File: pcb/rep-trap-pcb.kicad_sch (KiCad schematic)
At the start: 0 parts

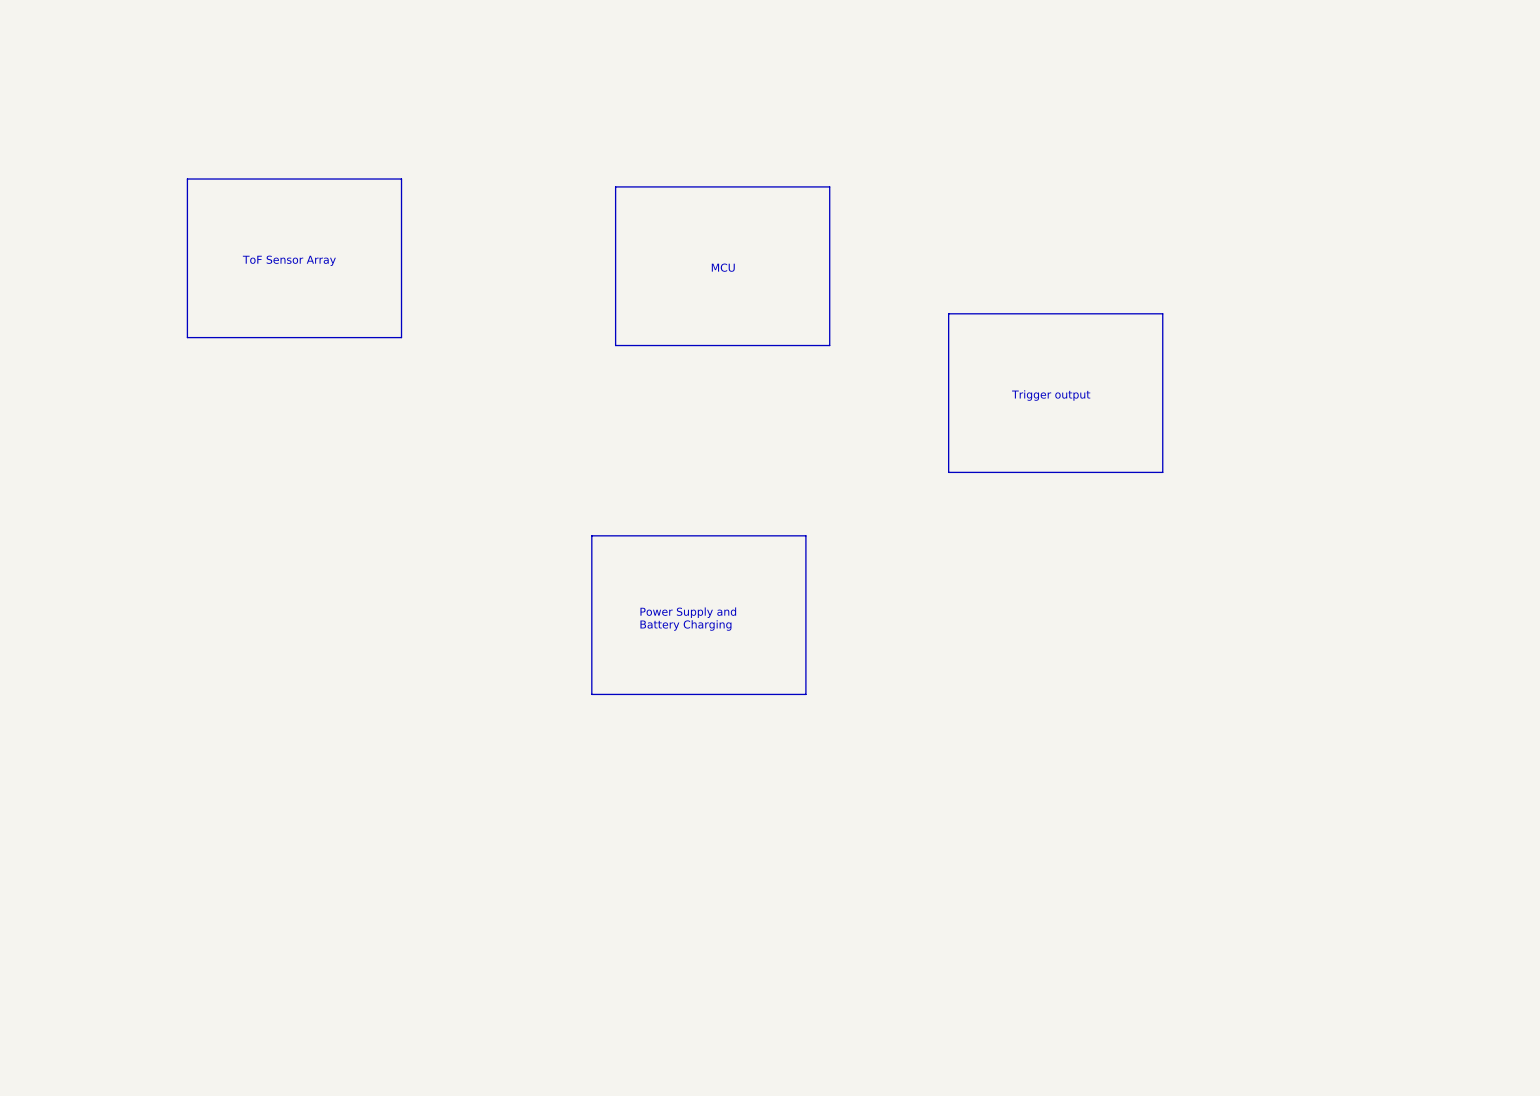
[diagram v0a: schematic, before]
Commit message: Added first components and size check
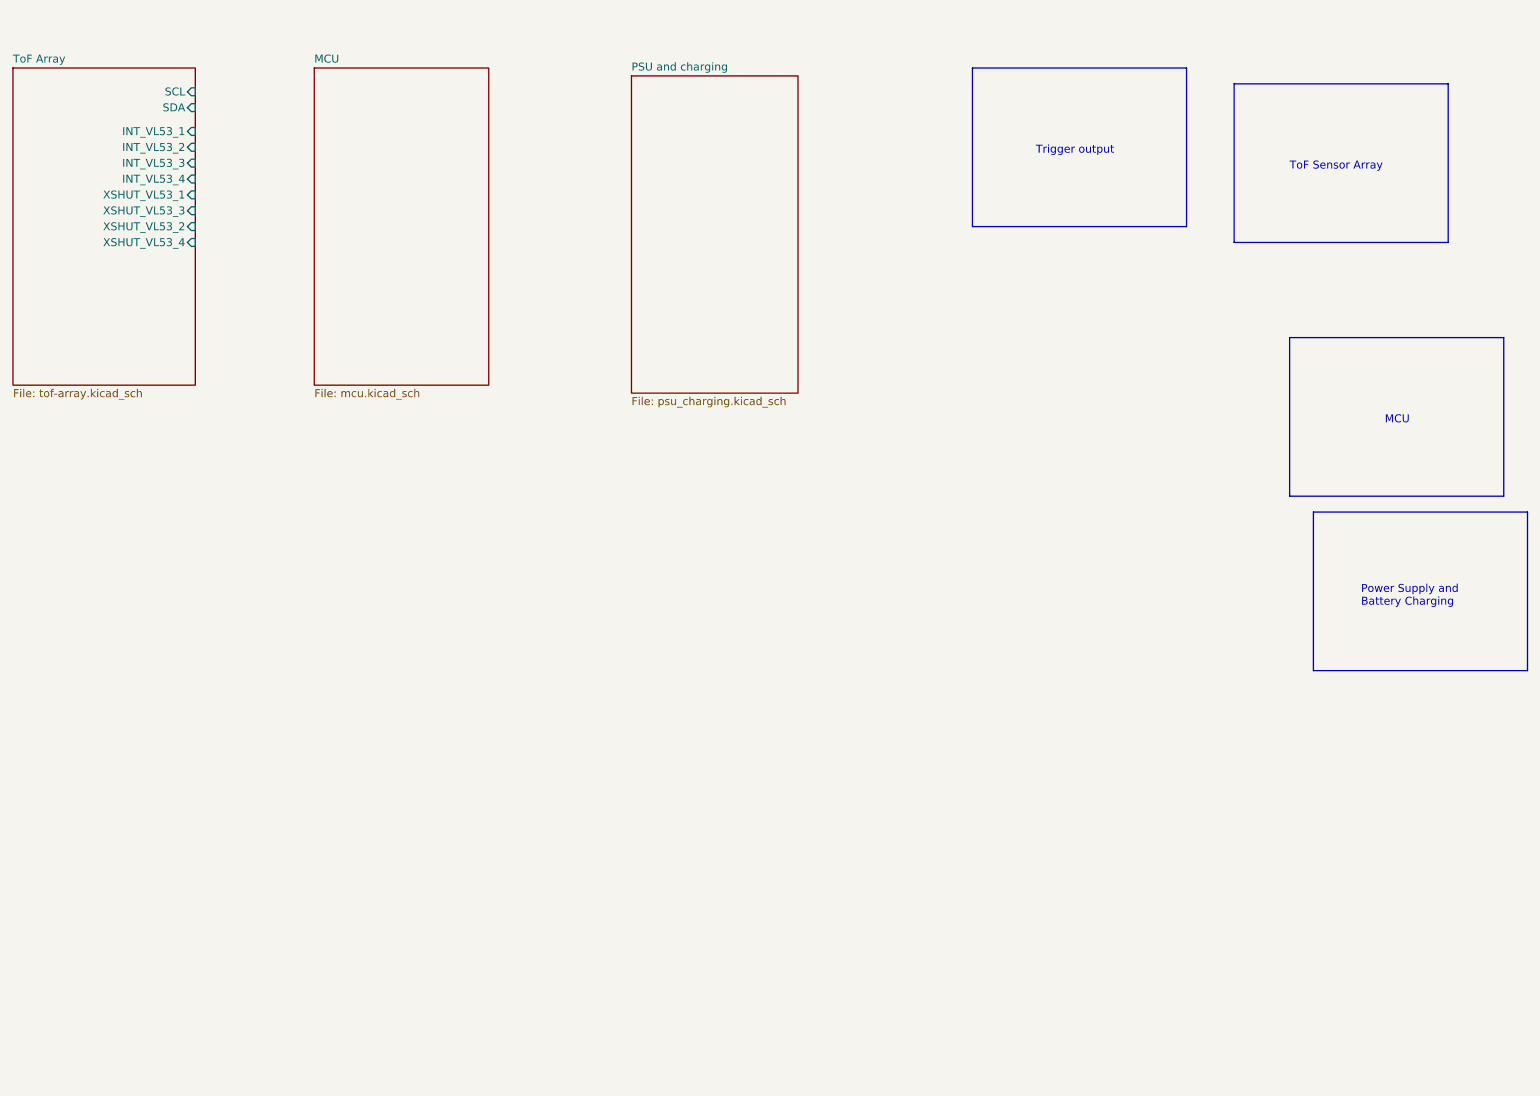
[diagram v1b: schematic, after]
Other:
- added sheet MCU (mcu.kicad_sch)
- added sheet PSU and charging (psu_charging.kicad_sch)
- added sheet ToF Array (tof-array.kicad_sch)
- company: (none) -> open-things
- title: (none) -> Passthrough Trigger Sensor
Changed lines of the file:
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@@
 (kicad_sch (version 20230121) (generator eeschema)
   (paper "A4")
-  (rectangle (start 124.46 105.41) (end 158.75 130.81)
+  (title_block
+    (title "Passthrough Trigger Sensor")
+    (date "2023-07-02")
+    (rev "rev01")
+    (company "open-things")
+  )
+  (rectangle (start 240.03 101.6) (end 274.32 127)
     (stroke (width 0) (type default))
     (fill (type none))
   )
-  (rectangle (start 181.61 69.85) (end 215.9 95.25)
+  (rectangle (start 185.42 30.48) (end 219.71 55.88)
     (stroke (width 0) (type default))
     (fill (type none))
   )
-  (rectangle (start 128.27 49.53) (end 162.56 74.93)
+  (rectangle (start 236.22 73.66) (end 270.51 99.06)
     (stroke (width 0) (type default))
     (fill (type none))
   )
-  (rectangle (start 59.69 48.26) (end 93.98 73.66)
+  (rectangle (start 227.33 33.02) (end 261.62 58.42)
     (stroke (width 0) (type default))
     (fill (type none))
   )
-  (text "Power Supply and \nBattery Charging" (at 132.08 120.65 0)
+  (text "Power Supply and \nBattery Charging" (at 247.65 116.84 0)
     (effects (font (size 1.27 1.27)) (justify left bottom))
   )
-  (text "ToF Sensor Array" (at 68.58 62.23 0)
+  (text "ToF Sensor Array" (at 236.22 46.99 0)
     (effects (font (size 1.27 1.27)) (justify left bottom))
   )
-  (text "Trigger output" (at 191.77 83.82 0)
+  (text "Trigger output" (at 195.58 44.45 0)
     (effects (font (size 1.27 1.27)) (justify left bottom))
   )
-  (text "MCU" (at 143.51 63.5 0)
+  (text "MCU" (at 251.46 87.63 0)
     (effects (font (size 1.27 1.27)) (justify left bottom))
   )
+  (sheet (at 31.75 30.48) (size 29.21 50.8) (fields_autoplaced)
+    (stroke (width 0.1524) (type solid))
+    (fill (color 0 0 0 0.0000))
+    (property "Sheetname" "ToF Array" (at 31.75 29.7684 0)
+      (effects (font (size 1.27 1.27)) (justify left bottom))
+    )
+    (property "Sheetfile" "tof-array.kicad_sch" (at 31.75 81.8646 0)
+      (effects (font (size 1.27 1.27)) (justify left top))
+    )
+    (pin "SCL" input (at 60.96 34.29 0)
+      (effects (font (size 1.27 1.27)) (justify right))
+    )
+    (pin "SDA" input (at 60.96 36.83 0)
+      (effects (font (size 1.27 1.27)) (justify right))
+    )
+    (pin "INT_VL53_1" input (at 60.96 40.64 0)
+      (effects (font (size 1.27 1.27)) (justify right))
+    )
+    (pin "INT_VL53_2" input (at 60.96 43.18 0)
+      (effects (font (size 1.27 1.27)) (justify right))
+    )
+    (pin "INT_VL53_3" input (at 60.96 45.72 0)
+      (effects (font (size 1.27 1.27)) (justify right))
+    )
+    (pin "INT_VL53_4" input (at 60.96 48.26 0)
+      (effects (font (size 1.27 1.27)) (justify right))
+    )
+    (pin "XSHUT_VL53_1" input (at 60.96 50.8 0)
+      (effects (font (size 1.27 1.27)) (justify right))
+    )
+    (pin "XSHUT_VL53_3" input (at 60.96 53.34 0)
+      (effects (font (size 1.27 1.27)) (justify right))
+    )
+    (pin "XSHUT_VL53_2" input (at 60.96 55.88 0)
+      (effects (font (size 1.27 1.27)) (justify right))
+    )
+    (pin "XSHUT_VL53_4" input (at 60.96 58.42 0)
+      (effects (font (size 1.27 1.27)) (justify right))
+    )
+    (instances
+      (project "rep-trap-pcb"
+        (path "/b363dc8f-4a45-4779-a397-ccb82393dab8" (page "2"))
+      )
+    )
+  )
+  (sheet (at 130.81 31.75) (size 26.67 50.8) (fields_autoplaced)
+    (stroke (width 0.1524) (type solid))
+    (fill (color 0 0 0 0.0000))
+    (property "Sheetname" "PSU and charging" (at 130.81 31.0384 0)
+      (effects (font (size 1.27 1.27)) (justify left bottom))
+    )
+    (property "Sheetfile" "psu_charging.kicad_sch" (at 130.81 83.1346 0)
+      (effects (font (size 1.27 1.27)) (justify left top))
+    )
+    (instances
+      (project "rep-trap-pcb"
+        (path "/b363dc8f-4a45-4779-a397-ccb82393dab8" (page "4"))
+      )
+    )
+  )
+  (sheet (at 80.01 30.48) (size 27.94 50.8) (fields_autoplaced)
+    (stroke (width 0.1524) (type solid))
+    (fill (color 0 0 0 0.0000))
+    (property "Sheetname" "MCU" (at 80.01 29.7684 0)
+      (effects (font (size 1.27 1.27)) (justify left bottom))
+    )
+    (property "Sheetfile" "mcu.kicad_sch" (at 80.01 81.8646 0)
+      (effects (font (size 1.27 1.27)) (justify left top))
+    )
+    (instances
+      (project "rep-trap-pcb"
+        (path "/b363dc8f-4a45-4779-a397-ccb82393dab8" (page "3"))
+      )
+    )
+  )
   (sheet_instances
